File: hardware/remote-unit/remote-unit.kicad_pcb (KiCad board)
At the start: 2 copper layers, 94 x 56.3 mm, 60 parts, among them J1 SOL_A, J2 RF Module, J3 ICSP, J5 SOL_B, J6 PWR 12V, J7 UART, J8 RS485, J9 SOLAR, Q1 N >1A@4VGS, Q2 PNP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

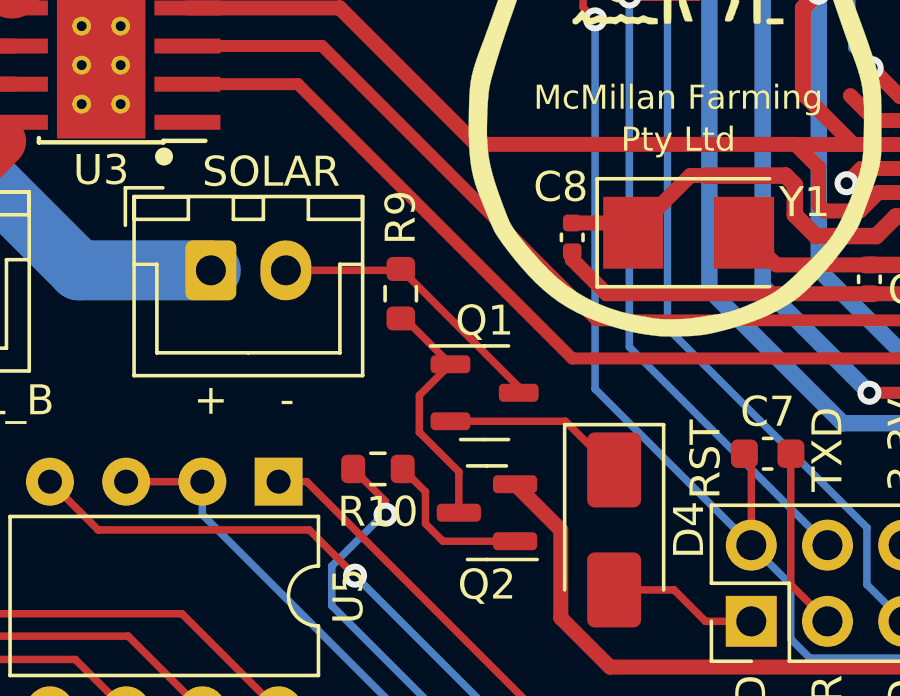
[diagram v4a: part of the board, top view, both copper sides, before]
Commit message: Fix remote unit charge control FET pin mismatch
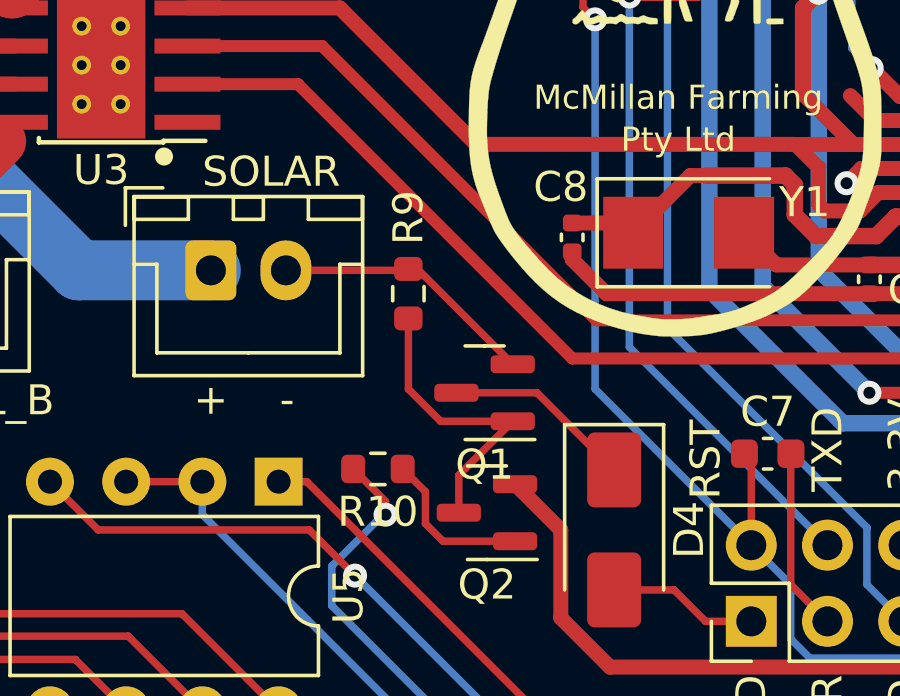
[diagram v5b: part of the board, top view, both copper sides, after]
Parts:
- Q1: footprint Package_TO_SOT_SMD:SOT-23-3 -> Package_TO_SOT_SMD:SOT-23
- moved R9 0.25 mm to (123.7, 106.9)
- turned Q1 to 180 degrees
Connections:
- Q1 pad 2: Net-(D4-K) -> /SOLAR_LOW
- Q1 pad 3: /SOLAR_LOW -> Net-(D4-K)
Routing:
- net Net-(Q1-G): track 8.21 -> 10.1 mm
- net /SOLAR_LOW: track 9.60 -> 8.90 mm
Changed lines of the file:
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@@
     )
   )
-  (footprint "Package_TO_SOT_SMD:SOT-23-3" (layer "F.Cu")
-    (at 126.238 110.236)
-    (descr "SOT, 3 Pin (https://www.jedec.org/sites/default/files/docs/Mo-178D.PDF inferred 3-pin variant), generated with kicad-footprint-generator ipc_gullwing_generator.py")
+  (footprint "Package_TO_SOT_SMD:SOT-23" (layer "F.Cu")
+    (at 126.238 110.236 180)
+    (descr "SOT, 3 Pin (https://www.jedec.org/system/files/docs/to-236h.pdf variant AB), generated with kicad-footprint-generator ipc_gullwing_generator.py")
     (tags "SOT TO_SOT_SMD")
     (property "JLCPCB Part" "C20917")
@@
     (property "Sheetfile" "remote-unit.kicad_sch")
     (property "Sheetname" "")
-    (property "ki_description" "30A Id, 55V Vds, 22mOhm Rds, N-Channel HEXFET Power MOSFET, TO-220AB")
+    (property "ki_description" "5.3A Id, 30V Vds, 27mOhm Rds, N-Channel HEXFET Power MOSFET, SOT-23")
     (property "ki_keywords" "N-Channel HEXFET MOSFET Logic-Level")
     (attr smd)
@@
     )
     (fp_text user "${REFERENCE}" (at 0 0) (layer "F.Fab")
-        (effects (font (size 0.4 0.4) (thickness 0.06)))
-    )
-    (fp_line (start 0 -1.56) (end -1.8 -1.56)
-      (stroke (width 0.12) (type solid)) (layer "F.SilkS"))
-    (fp_line (start 0 -1.56) (end 0.8 -1.56)
-      (stroke (width 0.12) (type solid)) (layer "F.SilkS"))
-    (fp_line (start 0 1.56) (end -0.8 1.56)
-      (stroke (width 0.12) (type solid)) (layer "F.SilkS"))
-    (fp_line (start 0 1.56) (end 0.8 1.56)
-      (stroke (width 0.12) (type solid)) (layer "F.SilkS"))
-    (fp_line (start -2.05 -1.7) (end -2.05 1.7)
-      (stroke (width 0.05) (type solid)) (layer "F.CrtYd"))
-    (fp_line (start -2.05 1.7) (end 2.05 1.7)
-      (stroke (width 0.05) (type solid)) (layer "F.CrtYd"))
-    (fp_line (start 2.05 -1.7) (end -2.05 -1.7)
-      (stroke (width 0.05) (type solid)) (layer "F.CrtYd"))
-    (fp_line (start 2.05 1.7) (end 2.05 -1.7)
-      (stroke (width 0.05) (type solid)) (layer "F.CrtYd"))
-    (fp_line (start -0.8 -1.05) (end -0.4 -1.45)
-      (stroke (width 0.1) (type solid)) (layer "F.Fab"))
-    (fp_line (start -0.8 1.45) (end -0.8 -1.05)
-      (stroke (width 0.1) (type solid)) (layer "F.Fab"))
-    (fp_line (start -0.4 -1.45) (end 0.8 -1.45)
-      (stroke (width 0.1) (type solid)) (layer "F.Fab"))
-    (fp_line (start 0.8 -1.45) (end 0.8 1.45)
-      (stroke (width 0.1) (type solid)) (layer "F.Fab"))
-    (fp_line (start 0.8 1.45) (end -0.8 1.45)
-      (stroke (width 0.1) (type solid)) (layer "F.Fab"))
-    (pad "1" smd roundrect (at -1.1375 -0.95) (size 1.325 0.6) (layers "F.Cu" "F.Paste" "F.Mask") (roundrect_rratio 0.25)
+        (effects (font (size 0.32 0.32) (thickness 0.05)))
+    )
+    (fp_line (start 0 -1.56) (end -1.675 -1.56)
+      (stroke (width 0.12) (type solid)) (layer "F.SilkS"))
+    (fp_line (start 0 -1.56) (end 0.65 -1.56)
+      (stroke (width 0.12) (type solid)) (layer "F.SilkS"))
+    (fp_line (start 0 1.56) (end -0.65 1.56)
+      (stroke (width 0.12) (type solid)) (layer "F.SilkS"))
+    (fp_line (start 0 1.56) (end 0.65 1.56)
+      (stroke (width 0.12) (type solid)) (layer "F.SilkS"))
+    (fp_line (start -1.92 -1.7) (end -1.92 1.7)
+      (stroke (width 0.05) (type solid)) (layer "F.CrtYd"))
+    (fp_line (start -1.92 1.7) (end 1.92 1.7)
+      (stroke (width 0.05) (type solid)) (layer "F.CrtYd"))
+    (fp_line (start 1.92 -1.7) (end -1.92 -1.7)
+      (stroke (width 0.05) (type solid)) (layer "F.CrtYd"))
+    (fp_line (start 1.92 1.7) (end 1.92 -1.7)
+      (stroke (width 0.05) (type solid)) (layer "F.CrtYd"))
+    (fp_line (start -0.65 -1.125) (end -0.325 -1.45)
+      (stroke (width 0.1) (type solid)) (layer "F.Fab"))
+    (fp_line (start -0.65 1.45) (end -0.65 -1.125)
+      (stroke (width 0.1) (type solid)) (layer "F.Fab"))
+    (fp_line (start -0.325 -1.45) (end 0.65 -1.45)
+      (stroke (width 0.1) (type solid)) (layer "F.Fab"))
+    (fp_line (start 0.65 -1.45) (end 0.65 1.45)
+      (stroke (width 0.1) (type solid)) (layer "F.Fab"))
+    (fp_line (start 0.65 1.45) (end -0.65 1.45)
+      (stroke (width 0.1) (type solid)) (layer "F.Fab"))
+    (pad "1" smd roundrect (at -0.9375 -0.95 180) (size 1.475 0.6) (layers "F.Cu" "F.Paste" "F.Mask") (roundrect_rratio 0.25)
       (net 44 "Net-(Q1-G)") (pinfunction "G") (pintype "input"))
-    (pad "2" smd roundrect (at -1.1375 0.95) (size 1.325 0.6) (layers "F.Cu" "F.Paste" "F.Mask") (roundrect_rratio 0.25)
+    (pad "2" smd roundrect (at -0.9375 0.95 180) (size 1.475 0.6) (layers "F.Cu" "F.Paste" "F.Mask") (roundrect_rratio 0.25)
+      (net 43 "/SOLAR_LOW") (pinfunction "S") (pintype "passive"))
+    (pad "3" smd roundrect (at 0.9375 0 180) (size 1.475 0.6) (layers "F.Cu" "F.Paste" "F.Mask") (roundrect_rratio 0.25)
       (net 29 "Net-(D4-K)") (pinfunction "D") (pintype "passive"))
-    (pad "3" smd roundrect (at 1.1375 0) (size 1.325 0.6) (layers "F.Cu" "F.Paste" "F.Mask") (roundrect_rratio 0.25)
-      (net 43 "/SOLAR_LOW") (pinfunction "S") (pintype "passive"))
-    (model "${KICAD6_3DMODEL_DIR}/Package_TO_SOT_SMD.3dshapes/SOT-23-3.wrl"
+    (model "${KICAD6_3DMODEL_DIR}/Package_TO_SOT_SMD.3dshapes/SOT-23.wrl"
       (offset (xyz 0 0 0))
       (scale (xyz 1 1 1))
@@
   )
   (footprint "Resistor_SMD:R_0603_1608Metric" (layer "F.Cu")
-    (at 123.444 106.934 90)
+    (at 123.698 106.934 90)
     (descr "Resistor SMD 0603 (1608 Metric), square (rectangular) end terminal, IPC_7351 nominal, (Body size source: IPC-SM-782 page 72, https://www.pcb-3d.com/wordpress/wp-content/uploads/ipc-sm-782a_amendment_1_and_2.pdf), generated with kicad-footprint-generator")
     (tags "resistor")
@@
   (segment (start 160.274 112.9625) (end 160.278 112.9665) (width 0.25) (layer "F.Cu") (net 28))
   (segment (start 160.274 111.48) (end 160.274 112.9625) (width 0.25) (layer "F.Cu") (net 28))
-  (segment (start 128.934 111.186) (end 130.556 112.808) (width 0.25) (layer "F.Cu") (net 29))
-  (segment (start 125.1005 111.186) (end 128.934 111.186) (width 0.25) (layer "F.Cu") (net 29))
+  (segment (start 125.3005 110.236) (end 127.984 110.236) (width 0.25) (layer "F.Cu") (net 29))
+  (segment (start 127.984 110.236) (end 130.556 112.808) (width 0.25) (layer "F.Cu") (net 29))
   (segment (start 90.852 80.598) (end 93.98 77.47) (width 1.7) (layer "B.Cu") (net 30))
   (segment (start 90.852 87.122) (end 90.852 80.598) (width 1.7) (layer "B.Cu") (net 30))
@@
   (segment (start 163.2204 116.1796) (end 157.988 121.412) (width 0.25) (layer "F.Cu") (net 42))
   (segment (start 161.8488 96.52) (end 163.2204 97.8916) (width 0.25) (layer "F.Cu") (net 42))
-  (segment (start 123.398 106.155) (end 123.444 106.109) (width 0.25) (layer "F.Cu") (net 43))
-  (segment (start 123.444 106.109) (end 127.3755 110.0405) (width 0.25) (layer "F.Cu") (net 43))
-  (segment (start 127.3755 110.0405) (end 127.3755 110.236) (width 0.25) (layer "F.Cu") (net 43))
-  (segment (start 119.614 106.155) (end 123.398 106.155) (width 0.25) (layer "F.Cu") (net 43))
-  (segment (start 125.379 114.234) (end 125.379 112.869462) (width 0.25) (layer "F.Cu") (net 44))
-  (segment (start 124.063 111.553462) (end 124.063 110.3235) (width 0.25) (layer "F.Cu") (net 44))
-  (segment (start 124.063 110.3235) (end 125.1005 109.286) (width 0.25) (layer "F.Cu") (net 44))
-  (segment (start 123.5735 107.759) (end 125.1005 109.286) (width 0.25) (layer "F.Cu") (net 44))
-  (segment (start 125.379 112.869462) (end 124.063 111.553462) (width 0.25) (layer "F.Cu") (net 44))
-  (segment (start 123.444 107.759) (end 123.5735 107.759) (width 0.25) (layer "F.Cu") (net 44))
+  (segment (start 123.652 106.155) (end 119.614 106.155) (width 0.25) (layer "F.Cu") (net 43))
+  (segment (start 123.698 106.109) (end 123.652 106.155) (width 0.25) (layer "F.Cu") (net 43))
+  (segment (start 123.9985 106.109) (end 123.698 106.109) (width 0.25) (layer "F.Cu") (net 43))
+  (segment (start 127.1755 109.286) (end 123.9985 106.109) (width 0.25) (layer "F.Cu") (net 43))
+  (segment (start 124.770538 111.186) (end 123.698 110.113462) (width 0.25) (layer "F.Cu") (net 44))
+  (segment (start 125.379 112.9825) (end 127.1755 111.186) (width 0.25) (layer "F.Cu") (net 44))
+  (segment (start 125.379 114.234) (end 125.379 112.9825) (width 0.25) (layer "F.Cu") (net 44))
+  (segment (start 127.1755 111.186) (end 124.770538 111.186) (width 0.25) (layer "F.Cu") (net 44))
+  (segment (start 123.698 110.113462) (end 123.698 107.759) (width 0.25) (layer "F.Cu") (net 44))
   (segment (start 124.2665 113.5355) (end 124.2665 114.601462) (width 0.25) (layer "F.Cu") (net 45))
   (segment (start 124.849038 115.184) (end 127.254 115.184) (width 0.25) (layer "F.Cu") (net 45))

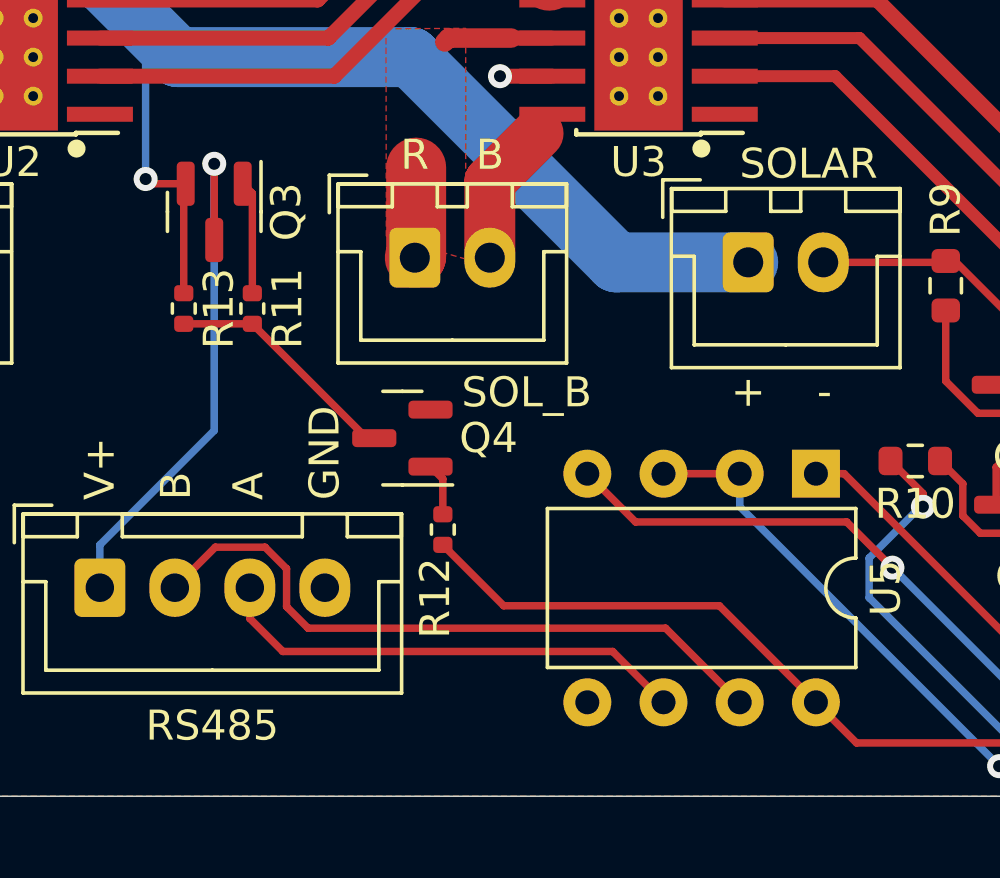
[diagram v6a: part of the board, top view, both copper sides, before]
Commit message: Fix remote unit rs485 sensor power supply circuit
Replace BJT with mosfet with appropriate source-gate voltage rating
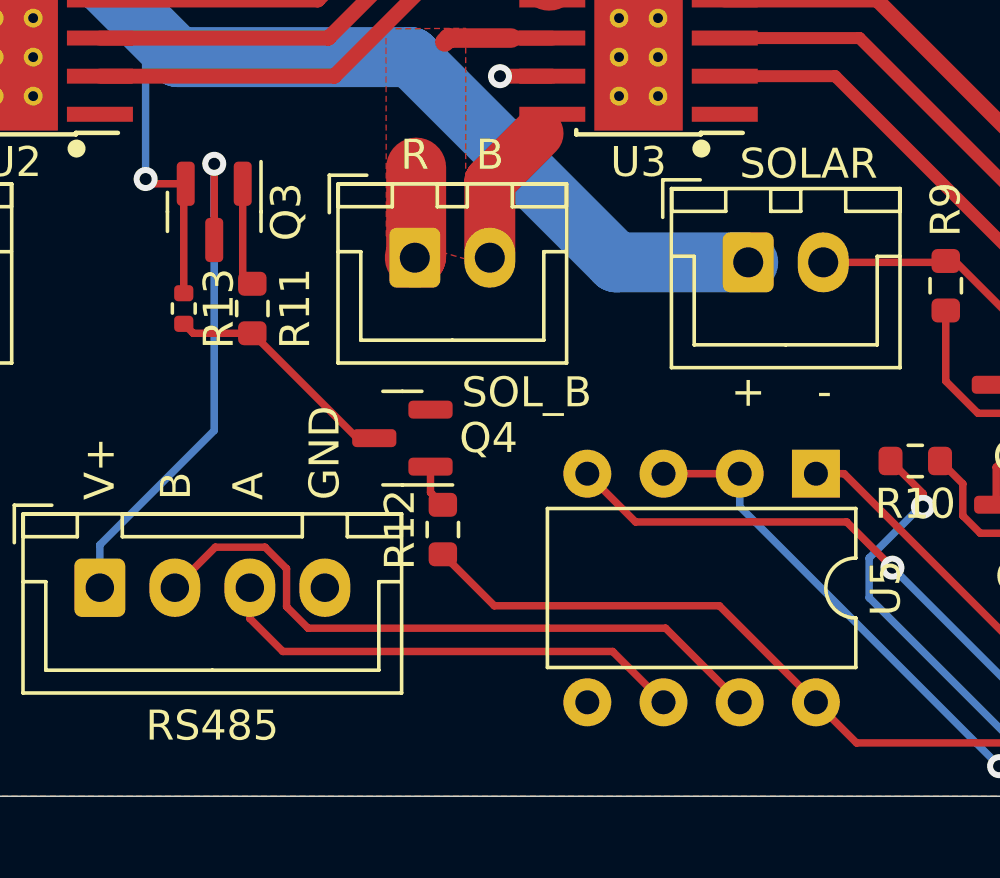
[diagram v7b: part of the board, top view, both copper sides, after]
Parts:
- Q3: value PNP -> VGS<-14v
- R11: value 10k -> 750; footprint Resistor_SMD:R_0402_1005Metric -> Resistor_SMD:R_0603_1608Metric
- R12: value 10k -> 3k; footprint Resistor_SMD:R_0402_1005Metric -> Resistor_SMD:R_0603_1608Metric
- R13: value 20k -> 10k

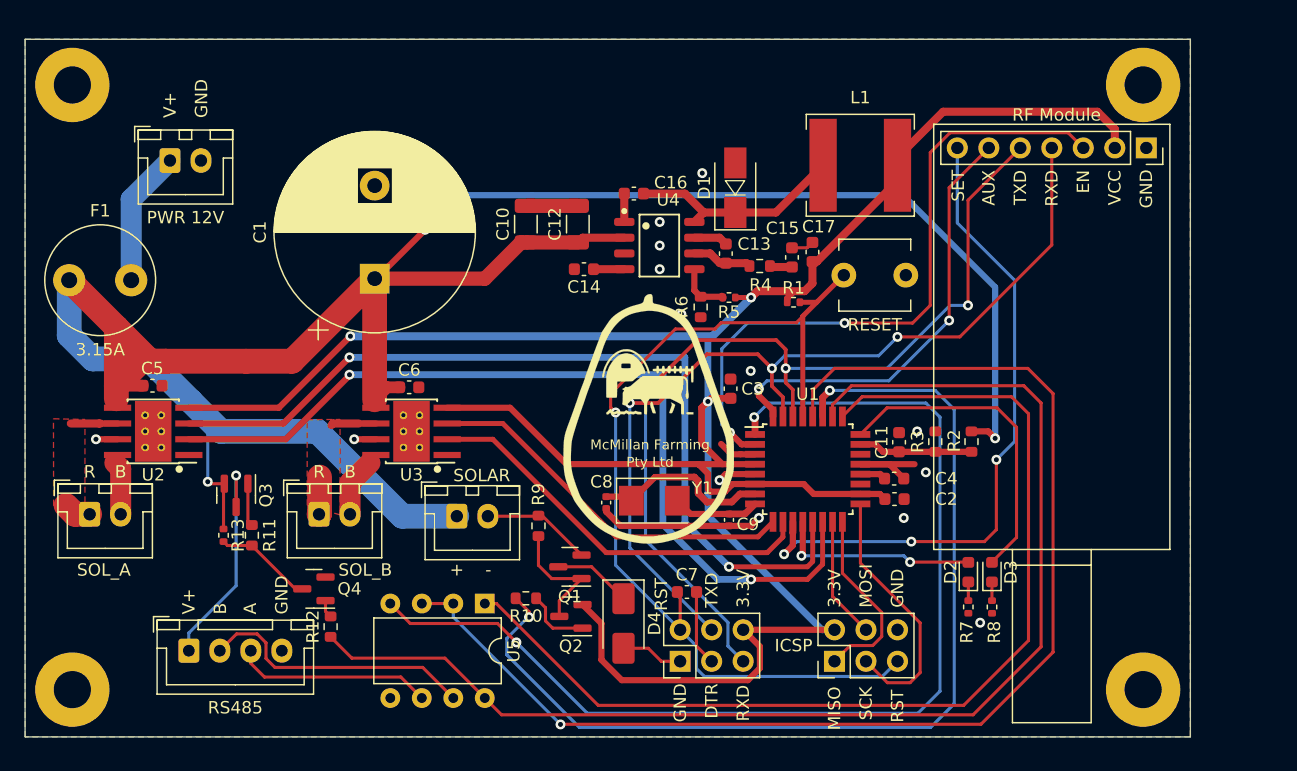
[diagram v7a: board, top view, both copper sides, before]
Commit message: Update remote unit buck converter
Update compensation network values.
Redo layout.
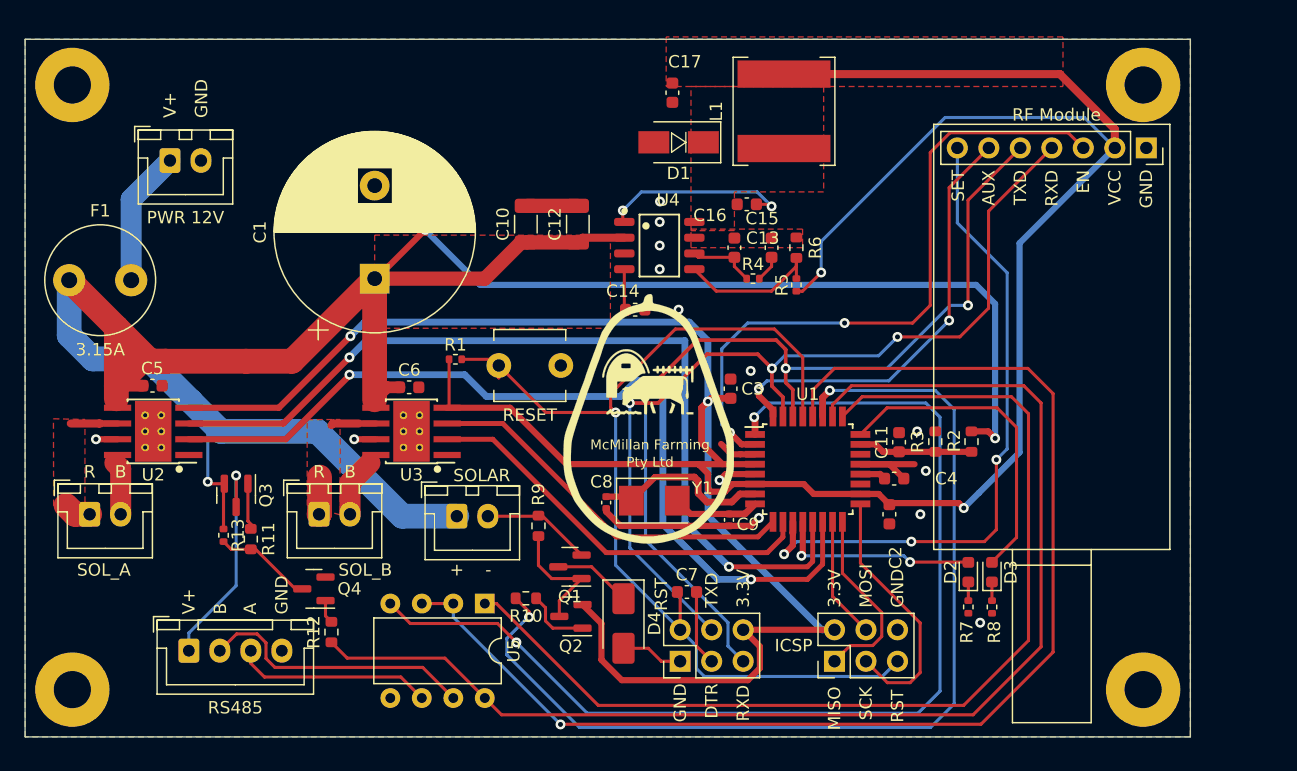
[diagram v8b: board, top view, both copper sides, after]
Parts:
- C13: value 6.8nF -> 10pF
- C15: value 22nF 25V -> 1.5nF 25V
- R4: value 750 -> 20k; footprint Resistor_SMD:R_0603_1608Metric -> Resistor_SMD:R_0402_1005Metric
- moved SW1 28.8 mm to (123.0, 94.0)
- moved R1 27.7 mm to (117.0, 93.5)
- moved C17 17.1 mm to (134.5, 72.0), turned to -90 degrees
- moved C16 9.15 mm to (140.5, 81.0), turned to 0 degrees
- moved R6 9.08 mm to (144.5, 84.5), turned to 90 degrees
- moved L1 7.54 mm to (143.5, 73.5), turned to 90 degrees
- moved D1 5.86 mm to (135.0, 76.0), turned to 180 degrees
- moved R5 5.53 mm to (144.5, 87.5), turned to 90 degrees
- moved C14 5.27 mm to (131.5, 89.5), turned to 0 degrees
- moved C15 1.82 mm to (142.5, 84.5)
- moved C2 1.29 mm to (152.0, 106.0), turned to -90 degrees
- moved R4 1.16 mm to (141.0, 87.0)
- moved C13 0.84 mm to (139.5, 84.5)
- moved R12 0.44 mm to (107.0, 115.5)
- moved R11 0.32 mm to (100.5, 108.0)
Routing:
- net +3.3V: track 202.7 -> 264.4 mm, vias 3 -> 4
- net Net-(D1-K): track 17.8 -> 0.00 mm
- net Net-(U4-BOOT): track 2.29 -> 15.4 mm, vias 0 -> 2
- net Net-(U4-VSENSE): track 4.24 -> 12.1 mm
- net /RESET: track 77.4 -> 84.2 mm
- net GND: track 44.9 -> 40.4 mm
- net +12V: track 199.9 -> 196.8 mm
- net /DRV_A1: track 70.7 -> 72.6 mm
- net Net-(U4-SS): track 2.48 -> 3.31 mm
- net Net-(U4-COMP): track 4.87 -> 5.49 mm
- net /DRV_A2: track 71.1 -> 71.8 mm
- added copper zone on F.Cu, net +12V
- added copper zone on F.Cu, net +3.3V
- added copper zone on F.Cu, net Net-(D1-K)
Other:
- board text added: "Daniel McMillan 2025"
- board text removed: "Daniel McMillan 2023"
